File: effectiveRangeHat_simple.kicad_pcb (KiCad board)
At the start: 8 copper layers, 30.6 x 66.8 mm, 120 parts, among them J1 Raspberry_Pi_2_3, J10 Conn_02x08_Odd_Even, J11 Conn_01x08, J2 BATT_CON, J3 PWR_HDR, J5 PeriHDR, J7 PWR_HDR, P1 USB4105GFA120, Q1 CSD13381F4, Q2 CSD13381F4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

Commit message: Bumping release from 1.10.1 to 1.11.0
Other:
- board text added: "MrHat v1.11.0"
- board text removed: "MrHat v1.10.1"
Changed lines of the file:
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@@
 	(title_block
 		(title "Effective Range: MrHat")
-		(date "2024-06-17")
-		(rev "1.10.1")
+		(date "2024-07-24")
+		(rev "1.11.0")
 		(company "Effective Range Kft.")
 		(comment 1 "visit https://creativecommons.org/licenses/by/4.0/")
@@
 		(layer "F.SilkS")
 	)
-	(gr_text "MrHat v1.10.1"
+	(gr_text "MrHat v1.11.0"
 		(at 108.458 108.6612 90)
 		(layer "B.Cu")

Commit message: Bumping release from 1.11.0 to 1.11.1
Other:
- board text added: "MrHat v1.11.1"
- board text removed: "MrHat v1.11.0"
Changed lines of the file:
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@@
 	(title_block
 		(title "Effective Range: MrHat")
-		(date "2024-07-24")
-		(rev "1.11.0")
+		(date "2024-08-14")
+		(rev "1.11.1")
 		(company "Effective Range Kft.")
 		(comment 1 "visit https://creativecommons.org/licenses/by/4.0/")
@@
 		(layer "F.SilkS")
 	)
-	(gr_text "MrHat v1.11.0"
+	(gr_text "MrHat v1.11.1"
 		(at 108.458 108.6612 90)
 		(layer "B.Cu")

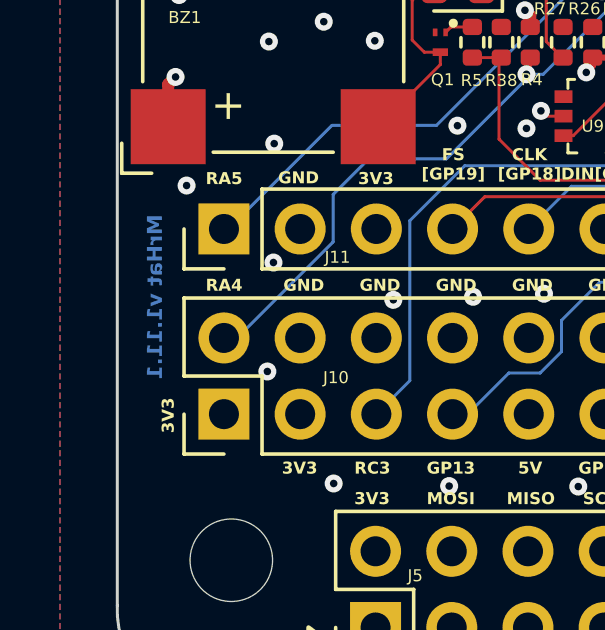
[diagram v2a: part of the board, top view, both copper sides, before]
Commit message: Bumping release from 1.11.1 to 1.11.2
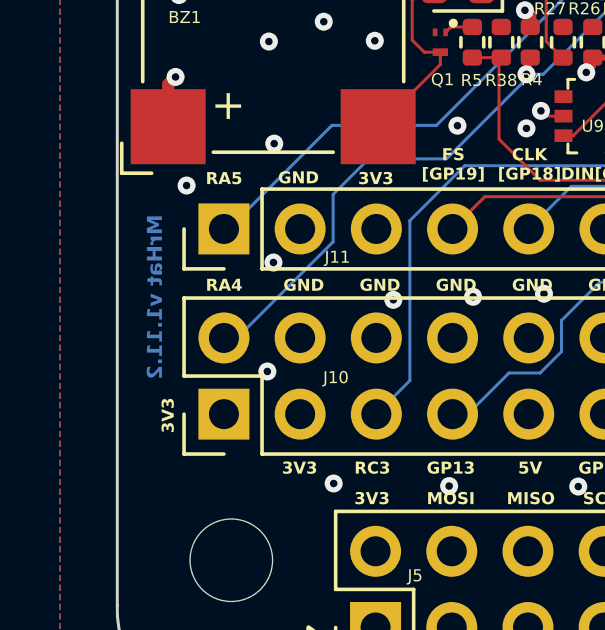
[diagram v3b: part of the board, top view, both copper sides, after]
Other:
- board text added: "MrHat v1.11.2"
- board text removed: "MrHat v1.11.1"
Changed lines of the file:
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@@
 		(title "Effective Range: MrHat")
 		(date "2024-08-14")
-		(rev "1.11.1")
+		(rev "1.11.2")
 		(company "Effective Range Kft.")
 		(comment 1 "visit https://creativecommons.org/licenses/by/4.0/")
@@
 		(layer "F.SilkS")
 	)
-	(gr_text "MrHat v1.11.1"
+	(gr_text "MrHat v1.11.2"
 		(at 108.458 108.6612 90)
 		(layer "B.Cu")

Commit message: fix: drc error
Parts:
- R8: value 5k1 -> 5k3
- R9: value 29k4 -> 30k1
